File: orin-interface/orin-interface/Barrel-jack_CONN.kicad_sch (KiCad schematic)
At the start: 1 part, among them J1 694108301002

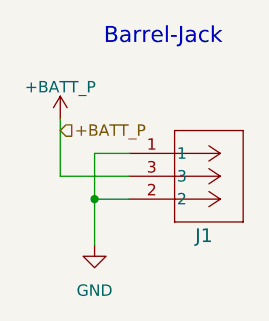
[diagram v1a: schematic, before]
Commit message: orin-interface: add ETH connector sheets and Mate-connectors footprint lib; update orin-bob
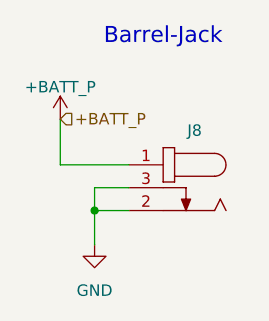
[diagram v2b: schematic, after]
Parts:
- removed J1: 694108301002, 694108301002:CONN3_01002_WRE, symbol 694108301002:694108301002
- added J8: 694106402002, 694106402002:J_Wurth_WR-DC_694106402002, symbol 694106402002:694106402002
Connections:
- net +BATT_P: now also J8.1
- net GND: now also J8.2, J8.3
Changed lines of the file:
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@@
 	)
 	(junction
-		(at 93.98 69.85)
+		(at 93.98 71.12)
 		(diameter 0)
 		(color 0 0 0 0)
@@
 	(wire
 		(pts
-			(xy 97.79 64.77) (xy 93.98 64.77)
-		)
-		(stroke
-			(width 0)
-			(type default)
-		)
-	)
-	(wire
-		(pts
-			(xy 93.98 69.85) (xy 97.79 69.85)
-		)
-		(stroke
-			(width 0)
-			(type default)
-		)
-	)
-	(wire
-		(pts
-			(xy 93.98 64.77) (xy 93.98 69.85)
-		)
-		(stroke
-			(width 0)
-			(type default)
-		)
-	)
-	(wire
-		(pts
-			(xy 97.79 67.31) (xy 90.17 67.31)
-		)
-		(stroke
-			(width 0)
-			(type default)
-		)
-	)
-	(wire
-		(pts
-			(xy 90.17 60.96) (xy 90.17 67.31)
-		)
-		(stroke
-			(width 0)
-			(type default)
-		)
-	)
-	(wire
-		(pts
-			(xy 93.98 69.85) (xy 93.98 74.93)
+			(xy 93.98 68.58) (xy 97.79 68.58)
+		)
+		(stroke
+			(width 0)
+			(type default)
+		)
+	)
+	(wire
+		(pts
+			(xy 93.98 71.12) (xy 97.79 71.12)
+		)
+		(stroke
+			(width 0)
+			(type default)
+		)
+	)
+	(wire
+		(pts
+			(xy 93.98 71.12) (xy 93.98 74.93)
+		)
+		(stroke
+			(width 0)
+			(type default)
+		)
+	)
+	(wire
+		(pts
+			(xy 97.79 66.04) (xy 90.17 66.04)
+		)
+		(stroke
+			(width 0)
+			(type default)
+		)
+	)
+	(wire
+		(pts
+			(xy 90.17 60.96) (xy 90.17 66.04)
+		)
+		(stroke
+			(width 0)
+			(type default)
+		)
+	)
+	(wire
+		(pts
+			(xy 93.98 68.58) (xy 93.98 71.12)
 		)
 		(stroke
@@
 	(hierarchical_label "+BATT_P"
 		(shape input)
-		(at 90.17 62.23 0)
+		(at 90.17 60.96 0)
 		(effects
 			(font
@@
 	)
 	(symbol
-		(lib_id "694108301002:694108301002")
-		(at 97.79 64.77 0)
+		(lib_id "694106402002:694106402002")
+		(at 104.14 67.31 0)
+		(mirror y)
 		(unit 1)
 		(body_style 1)
@@
 		(in_pos_files yes)
 		(dnp no)
-		(property "Reference" "J1"
-			(at 105.156 73.914 0)
-			(show_name no)
-			(do_not_autoplace no)
-			(effects
-				(font
-					(size 1.524 1.524)
-				)
-				(justify left)
-			)
-		)
-		(property "Value" "694108301002"
-			(at 111.76 68.5799 0)
-			(hide yes)
-			(show_name no)
-			(do_not_autoplace no)
-			(effects
-				(font
-					(size 1.524 1.524)
-				)
-				(justify left)
-			)
-		)
-		(property "Footprint" "694108301002:CONN3_01002_WRE"
-			(at 97.79 64.77 0)
-			(hide yes)
-			(show_name no)
-			(do_not_autoplace no)
-			(effects
-				(font
-					(size 1.27 1.27)
-					(italic yes)
-				)
-			)
-		)
-		(property "Datasheet" "https://www.we-online.com/catalog/datasheet/694108301002.pdf"
-			(at 97.79 64.77 0)
-			(hide yes)
-			(show_name no)
-			(do_not_autoplace no)
-			(effects
-				(font
-					(size 1.27 1.27)
-					(italic yes)
-				)
-			)
-		)
-		(property "Description" ""
-			(at 97.79 64.77 0)
-			(hide yes)
-			(show_name no)
-			(do_not_autoplace no)
-			(effects
-				(font
-					(size 1.27 1.27)
-				)
+		(property "Reference" "J8"
+			(at 105.0925 62.23 0)
+			(show_name no)
+			(do_not_autoplace no)
+			(effects
+				(font
+					(size 1.27 1.27)
+				)
+			)
+		)
+		(property "Value" "694106402002"
+			(at 91.44 44.45 0)
+			(hide yes)
+			(show_name no)
+			(do_not_autoplace no)
+			(effects
+				(font
+					(size 1.27 1.27)
+				)
+				(justify left)
+			)
+		)
+		(property "Footprint" "694106402002:J_Wurth_WR-DC_694106402002"
+			(at 91.44 46.99 0)
+			(hide yes)
+			(show_name no)
+			(do_not_autoplace no)
+			(effects
+				(font
+					(size 1.27 1.27)
+				)
+				(justify left)
+			)
+		)
+		(property "Datasheet" "https://www.we-online.com/catalog/datasheet/694106402002.pdf?ki"
+			(at 91.44 49.53 0)
+			(hide yes)
+			(show_name no)
+			(do_not_autoplace no)
+			(effects
+				(font
+					(size 1.27 1.27)
+				)
+				(justify left)
+			)
+		)
+		(property "Description" "Power Jacks ED"
+			(at 104.14 67.31 0)
+			(hide yes)
+			(show_name no)
+			(do_not_autoplace no)
+			(effects
+				(font
+					(size 1.27 1.27)
+				)
+			)
+		)
+		(property "Manufacturer" "Wurth Elektronik"
+			(at 91.44 52.07 0)
+			(hide yes)
+			(show_name no)
+			(do_not_autoplace no)
+			(effects
+				(font
+					(size 1.27 1.27)
+				)
+				(justify left)
+			)
+		)
+		(property "Manufacturer URL" "https://www.we-online.com"
+			(at 91.44 54.61 0)
+			(hide yes)
+			(show_name no)
+			(do_not_autoplace no)
+			(effects
+				(font
+					(size 1.27 1.27)
+				)
+				(justify left)
+			)
+		)
+		(property "Created Date" "20251209"
+			(at 91.44 57.15 0)
+			(hide yes)
+			(show_name no)
+			(do_not_autoplace no)
+			(effects
+				(font
+					(size 1.27 1.27)
+				)
+				(justify left)
+			)
+		)
+		(property "Series" "WR-DC"
+			(at 91.44 59.69 0)
+			(hide yes)
+			(show_name no)
+			(do_not_autoplace no)
+			(effects
+				(font
+					(size 1.27 1.27)
+				)
+				(justify left)
+			)
+		)
+		(property "Part Number" "694106402002"
+			(at 91.44 62.23 0)
+			(hide yes)
+			(show_name no)
+			(do_not_autoplace no)
+			(effects
+				(font
+					(size 1.27 1.27)
+				)
+				(justify left)
+			)
+		)
+		(property "Mounting Technology" "THT"
+			(at 91.44 64.77 0)
+			(hide yes)
+			(show_name no)
+			(do_not_autoplace no)
+			(effects
+				(font
+					(size 1.27 1.27)
+				)
+				(justify left)
+			)
+		)
+		(property "Center pin Ø (Value) (mm)" "2.0"
+			(at 91.44 67.31 0)
+			(hide yes)
+			(show_name no)
+			(do_not_autoplace no)
+			(effects
+				(font
+					(size 1.27 1.27)
+				)
+				(justify left)
+			)
+		)
+		(property "Plug OD (mm)" "5.5"
+			(at 91.44 69.85 0)
+			(hide yes)
+			(show_name no)
+			(do_not_autoplace no)
+			(effects
+				(font
+					(size 1.27 1.27)
+				)
+				(justify left)
+			)
+		)
+		(property "Type" "Vertical"
+			(at 91.44 72.39 0)
+			(hide yes)
+			(show_name no)
+			(do_not_autoplace no)
+			(effects
+				(font
+					(size 1.27 1.27)
+				)
+				(justify left)
+			)
+		)
+		(property "IR (A)" "3.0"
+			(at 91.44 74.93 0)
+			(hide yes)
+			(show_name no)
+			(do_not_autoplace no)
+			(effects
+				(font
+					(size 1.27 1.27)
+				)
+				(justify left)
+			)
+		)
+		(property "Working Voltage (V (DC))" "30"
+			(at 91.44 77.47 0)
+			(hide yes)
+			(show_name no)
+			(do_not_autoplace no)
+			(effects
+				(font
+					(size 1.27 1.27)
+				)
+				(justify left)
 			)
 		)
@@
 			(project "orin-interface"
 				(path "/18aef7c7-2f0e-4a2c-9e5d-7b655e80b6a3/20583298-77c4-4850-98ea-6d3ace102595"
-					(reference "J1")
+					(reference "J8")
 					(unit 1)
 				)
